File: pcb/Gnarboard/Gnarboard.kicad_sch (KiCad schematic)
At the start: 16 parts, among them J1 N2K, J2 I2C, J3 Screw_Terminal_01x09, J4 Screw_Terminal_01x09, U1 ESP32-DEVKITC, U2 MCP3208, U3 R-78B3.3-2.0

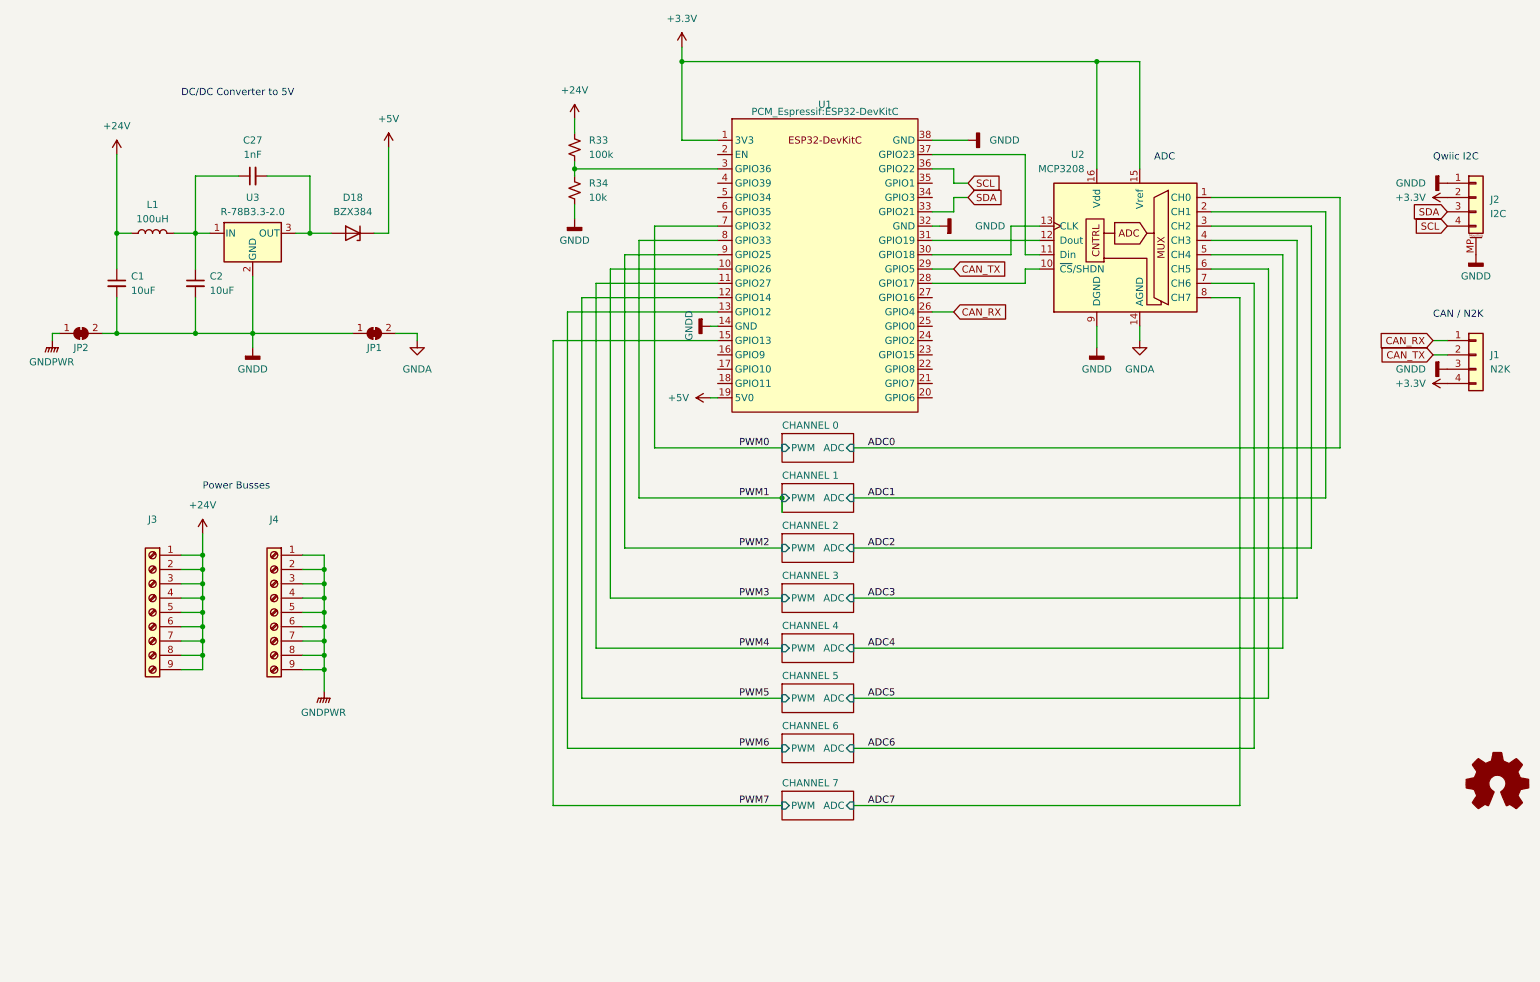
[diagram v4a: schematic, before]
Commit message: added a pwm fan output to the board.
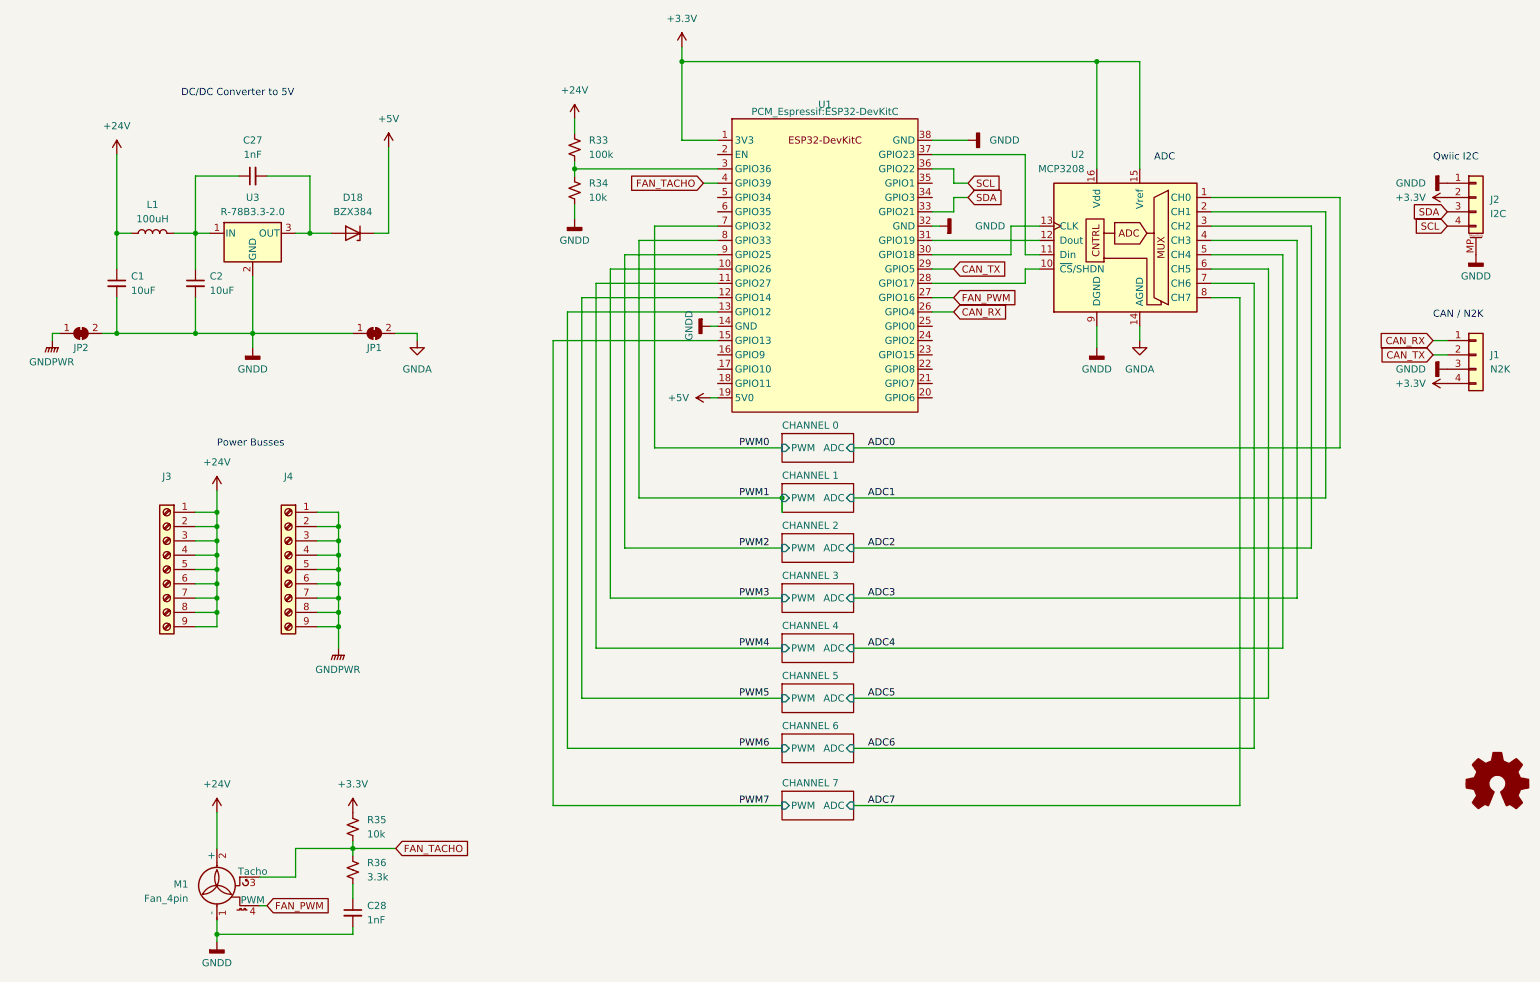
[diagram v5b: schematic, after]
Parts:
- added C28: 1nF, Capacitor_SMD:C_0805_2012Metric_Pad1.18x1.45mm_HandSolder, symbol Device:C_Small
- added M1: Fan_4pin, gnarboard:Molex 0470531000, symbol Motor:Fan_4pin
- added R35: 10k, Resistor_SMD:R_0805_2012Metric_Pad1.20x1.40mm_HandSolder, symbol Device:R_Small_US
- added R36: 3.3k, Resistor_SMD:R_0805_2012Metric_Pad1.20x1.40mm_HandSolder, symbol Device:R_Small_US
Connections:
- net +24V: now also M1.2 (+)
- net +3.3V: now also R35.2
- net GNDD: now also C28.2, M1.1 (-)
- net FAN_PWM: now reaches U1.27 (GPIO16)
- net FAN_PWM: now also M1.4 (PWM)
- net FAN_TACHO: now reaches U1.4 (GPIO39)
- net FAN_TACHO: now also M1.3 (Tacho), R35.1, R36.2
- new net: C28.1, R36.1
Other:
- moved on the sheet: J3, J4

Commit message: library for the power regulator was wrong.  oops.
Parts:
- U3: footprint Converter_DCDC:Converter_DCDC_RECOM_R-78B-2.0_THT -> gnarboard:RECOM R-78K
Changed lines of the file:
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@@
       (effects (font (size 1.27 1.27)))
     )
-    (property "Footprint" "Converter_DCDC:Converter_DCDC_RECOM_R-78B-2.0_THT" (at 55.88 67.31 0)
+    (property "Footprint" "gnarboard:RECOM R-78K" (at 55.88 67.31 0)
       (effects (font (size 1.27 1.27) italic) (justify left) hide)
     )
